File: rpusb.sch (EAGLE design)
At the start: 105 parts, among them IC1 M24C02-FMH6TG, IC2 RP2040, IC3 RP2040, IC4 16MB_Flash, IC5 16MB_Flash, IC6 AP7362-33SP-13, J2 Micro-B, J3 Micro-B

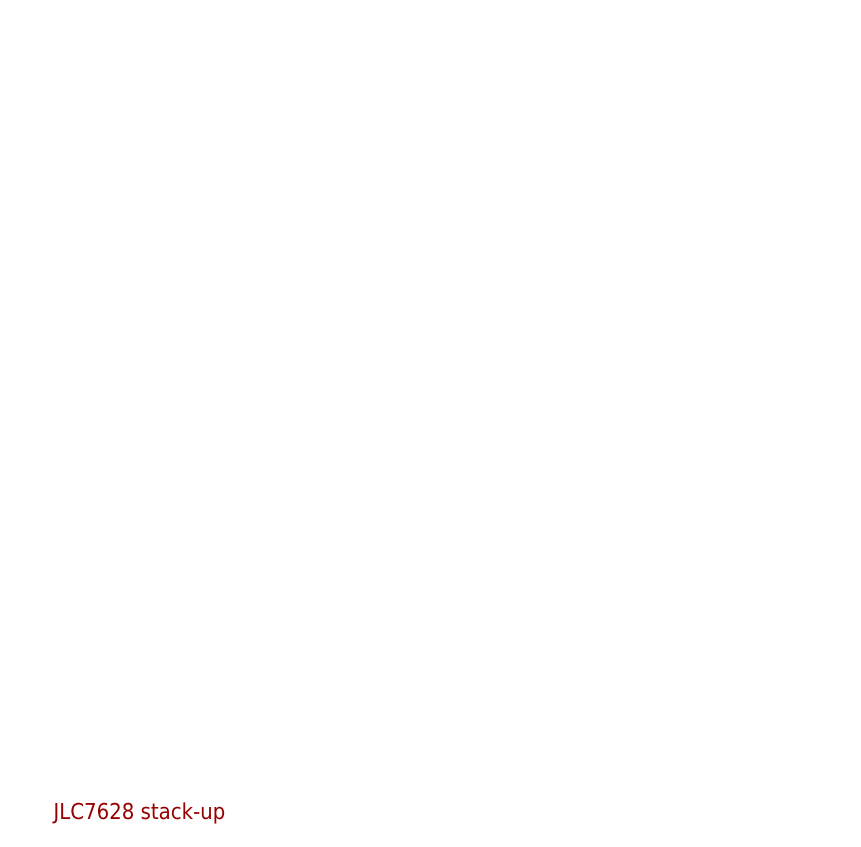
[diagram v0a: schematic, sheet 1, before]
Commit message: First stab at routing the board - set up for JCLPCB
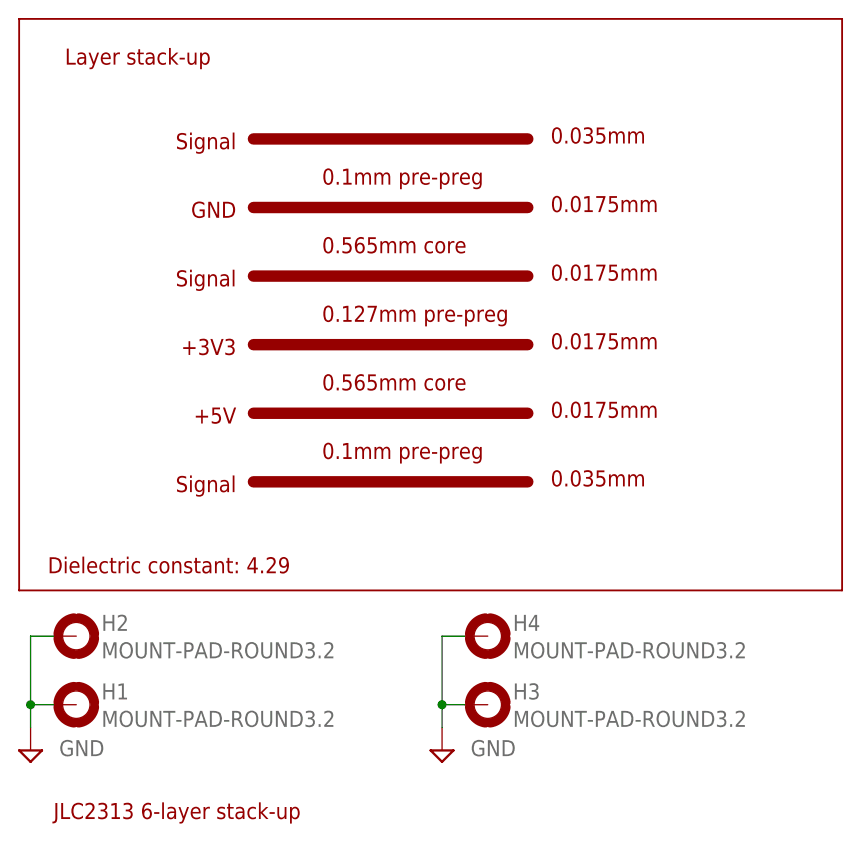
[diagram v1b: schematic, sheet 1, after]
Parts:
- removed J2, J3: Micro-B, samacsys:MCR-B-S-RA-SMT-CS14-T_R
- added H1, H2, H3, H4: MOUNT-PAD-ROUND3.2, holes:MOUNT-PAD-ROUND3.2
- added SPI_PROG: (no value), pinhead:PINHD-2X4
- added USB_IN1, USB_IN2: U254-051T-4BHJ25-S2S, samacsys:U254-051T-4BHJ25-S2S
- Q1, Q2, Q3: value (none) -> 12MHz
- USB_IN: value Micro-B -> U254-051T-4BHJ25-S2S; device samacsys:MCR-B-S-RA-SMT-CS14-T_R -> samacsys:U254-051T-4BHJ25-S2S; USE MCR-B-S-RA-SMT-CS14-T_R -> (none)
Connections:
- net !QSPI2_SS!: now also SPI_PROG.4
- net +5V: now also USB_IN1.VBUS@1, USB_IN2.VBUS@1; no longer J2.VBUS, J3.VBUS
- net GND: now also H1.MOUNT, H2.MOUNT, H3.MOUNT, H4.MOUNT, IC6.GND@1, USB_IN.GND@5, USB_IN1.GND@5, USB_IN1.MH1, USB_IN1.MH2, USB_IN1.MH3, USB_IN1.MH4, USB_IN2.GND@5, USB_IN2.MH1, USB_IN2.MH2, USB_IN2.MH3, USB_IN2.MH4; no longer J2.GND, J2.MH1, J2.MH2, J2.MH3, J2.MH4, J3.GND, J3.MH1, J3.MH2, J3.MH3, J3.MH4, USB_IN.GND
- net GPIO0: now also SPI_PROG.1
- net GPIO1: now also SPI_PROG.3
- net GPIO2: now also SPI_PROG.5
- net GPIO3: now also SPI_PROG.7
- net N$19: now also D6.-, D7.+
- net QSPI2_CLK: now also SPI_PROG.6
- net QSPI2_SD0: now also SPI_PROG.8
- net QSPI2_SD1: now also SPI_PROG.2
- net USB_D2_N: now also USB_IN2.D-@2; no longer J2.D-
- net USB_D2_P: now also USB_IN2.D+@3; no longer J2.D+
- net USB_D3_N: now also USB_IN1.D-@2; no longer J3.D-
- net USB_D3_P: now also USB_IN1.D+@3; no longer J3.D+
- net USB_N: now also USB_IN.D-@2; no longer USB_IN.D-
- net USB_P: now also USB_IN.D+@3; no longer USB_IN.D+
- net VBUS: now also USB_IN.VBUS@1; no longer USB_IN.VBUS
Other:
- note added: "+3V3"
- note added: "+5V"
- note added: "0.0175mm"
- note added: "0.035mm"
- note added: "0.127mm pre-preg"
- note added: "0.1mm pre-preg"
- note added: "0.565mm core"
- note added: "Dielectric constant: 4.29"
- note added: "GND"
- note added: "JLC2313 6-layer stack-up"
- note added: "Layer stack-up"
- note added: "Signal"
- note removed: "JLC7628 stack-up"

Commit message: Ready to order from NextPCB
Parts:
- added TP_3V3, TP_5V, TP_GND, TP_VBUS: S1751-46R, samacsys:S1751-46R
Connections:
- net +3V3_RP: now also TP_3V3.1
- net +5V: now also TP_5V.1
- net GND: now also GPIO_1.37, GPIO_1.38, TP_GND.1
- net VBUS: now also TP_VBUS.1
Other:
- note added: "0.195mm pre-preg (7628)"
- note added: "1.065mm core"
- note added: "USB traces 90R - 10 mil trace - 5 mil space"
- note removed: "+3V3"
- note removed: "+5V"
- note removed: "0.035mm"
- note removed: "0.127mm pre-preg"
- note removed: "0.1mm pre-preg"
- note removed: "0.565mm core"
